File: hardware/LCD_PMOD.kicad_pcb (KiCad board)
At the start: 2 copper layers, 185 x 95 mm, 34 parts, among them IC1 TPS61169DCKR, IC2 TPD4E001DRLR, IC3 AR1021-I/SS, J1 20-pin power socket, J2 Conn_02x14_Odd_Even, J3 28-pin module socket, J4 691327310016, J5 691327310016, U1 ADS8556IPM, U2 OPA2211AIDDA, U3 DS90CF364AMTD, U4 DS90CF363AMTD

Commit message: Assigning footprints
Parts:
- removed J2: Conn_02x14_Odd_Even, Connector_PinHeader_2.54mm:PinHeader_2x14_P2.54mm_Horizontal
- added C10: 100n, Capacitor_SMD:C_0603_1608Metric, F.Cu at (110.5, 106.9)
- added C11: 100n, Capacitor_SMD:C_0603_1608Metric, F.Cu at (104.6, 107.7)
- added C12: 100n, Capacitor_SMD:C_0603_1608Metric, F.Cu at (116.8, 107.2)
- added C13: 100n, Capacitor_SMD:C_0603_1608Metric, F.Cu at (108.2, 114.3)
- added C14: 100n, Capacitor_SMD:C_0603_1608Metric, F.Cu at (117.3, 114.8)
- added C15: 100n, Capacitor_SMD:C_0603_1608Metric, F.Cu at (121.9, 108.0)
- added C16: 100n, Capacitor_SMD:C_0603_1608Metric, F.Cu at (113.0, 110.7)
- added C17: 100n, Capacitor_SMD:C_0603_1608Metric, F.Cu at (221.2, 102.6)
- added C18: 100n, Capacitor_SMD:C_0603_1608Metric, F.Cu at (210.6, 115.1)
- added C19: 100n, Capacitor_SMD:C_0603_1608Metric, F.Cu at (202.2, 105.2)
- added C20: 100n, Capacitor_SMD:C_0603_1608Metric, F.Cu at (209.1, 103.8)
- added C21: 100n, Capacitor_SMD:C_0603_1608Metric, F.Cu at (193.3, 110.0)
- added C22: 100n, Capacitor_SMD:C_0603_1608Metric, F.Cu at (202.4, 110.0)
- added C23: 100n, Capacitor_SMD:C_0603_1608Metric, F.Cu at (210.6, 98.6)
- added C24: 100n, Capacitor_SMD:C_0603_1608Metric, F.Cu at (199.4, 115.6)
- added C25: 100n, Capacitor_SMD:C_0603_1608Metric, F.Cu at (221.2, 115.3)
- added C26: 100n, Capacitor_SMD:C_0603_1608Metric, F.Cu at (209.0, 109.2)
- added C27: 100n, Capacitor_SMD:C_0603_1608Metric, F.Cu at (218.9, 108.7)
- added C28: 100n, Capacitor_SMD:C_0603_1608Metric, F.Cu at (206.0, 96.8)
- added C29: 100n, Capacitor_SMD:C_0603_1608Metric, F.Cu at (215.6, 113.5)
- added C30: 100n, Capacitor_SMD:C_0603_1608Metric, F.Cu at (204.7, 115.3)
- added C31: 100n, Capacitor_SMD:C_0603_1608Metric, F.Cu at (200.9, 100.8)
- added C32: 100n, Capacitor_SMD:C_0603_1608Metric, F.Cu at (215.1, 101.3)
- added C33: 100n, Capacitor_SMD:C_0603_1608Metric, F.Cu at (153.8, 55.7)
- added C34: 100n, Capacitor_SMD:C_0603_1608Metric, F.Cu at (143.3, 55.8)
- added C35: 100n, Capacitor_SMD:C_0603_1608Metric, F.Cu at (150.4, 60.5)
- added C36: 100n, Capacitor_SMD:C_0603_1608Metric, F.Cu at (93.1, 107.4)
- added C37: 10uF, Capacitor_SMD:C_0603_1608Metric, F.Cu at (90.1, 114.4)
- added C38: 100n, Capacitor_SMD:C_0603_1608Metric, F.Cu at (85.3, 111.8)
- added C39: 100n, Capacitor_SMD:C_0603_1608Metric, F.Cu at (150.2, 55.7)
- added C40: 470n, Capacitor_SMD:C_0603_1608Metric, F.Cu at (147.4, 60.5)
- added C41: 100n, Capacitor_SMD:C_0603_1608Metric, F.Cu at (87.6, 107.7)
- added C42: 100n, Capacitor_SMD:C_0603_1608Metric, F.Cu at (147.1, 55.9)
- added C43: 100n, Capacitor_SMD:C_0603_1608Metric, F.Cu at (95.8, 110.5)
- added C44: 1uF, Capacitor_SMD:C_0603_1608Metric, F.Cu at (144.4, 60.5)
- added C45: 10uF, Capacitor_SMD:C_0603_1608Metric, F.Cu at (98.8, 106.9)
- added C46: 100n, Capacitor_SMD:C_0603_1608Metric, F.Cu at (153.4, 60.5)
- added C47: 100n, Capacitor_SMD:C_0603_1608Metric, F.Cu at (93.1, 114.4)
- added C48: 10uF, Capacitor_SMD:C_0603_1608Metric, F.Cu at (100.6, 111.8)
- added C49: 10uF, Capacitor_SMD:C_0603_1608Metric, F.Cu at (104.9, 111.3)
- added C50: 10uF, Capacitor_SMD:C_0603_1608Metric, F.Cu at (96.1, 114.4)
- added C51: 10uF, Capacitor_SMD:C_0603_1608Metric, F.Cu at (103.6, 76.2)
- added C52: 100n, Capacitor_SMD:C_0603_1608Metric, F.Cu at (90.8, 80.1)
- added C53: 1u, Capacitor_SMD:C_0603_1608Metric, F.Cu at (89.9, 76.2)
- added C54: 22u, Capacitor_SMD:C_0603_1608Metric, F.Cu at (94.2, 78.2)
- added C55: 47u, Capacitor_SMD:C_0603_1608Metric, F.Cu at (97.7, 74.6)
- added C56: 47u, Capacitor_SMD:C_0603_1608Metric, F.Cu at (104.4, 71.9)
- added C57: 10n, Capacitor_SMD:C_0603_1608Metric, F.Cu at (94.5, 71.9)
- added C58: 10n, Capacitor_SMD:C_0603_1608Metric, F.Cu at (101.3, 83.3)
- added C59: 47u, Capacitor_SMD:C_0603_1608Metric, F.Cu at (99.8, 78.5)
- added C60: NI, Capacitor_SMD:C_0603_1608Metric, F.Cu at (287.3, 99.6)
- added C61: NI, Capacitor_SMD:C_0603_1608Metric, F.Cu at (249.0, 92.0)
- added C62: 370pF, Capacitor_SMD:C_0603_1608Metric, F.Cu at (265.7, 98.6)
- added C63: 470p, Capacitor_SMD:C_0603_1608Metric, F.Cu at (258.1, 84.3)
- added C64: 470p, Capacitor_SMD:C_0603_1608Metric, F.Cu at (268.0, 82.8)
- added C65: 1n, Capacitor_SMD:C_0603_1608Metric, F.Cu at (295.7, 99.3)
- added C66: 1n, Capacitor_SMD:C_0603_1608Metric, F.Cu at (261.4, 91.4)
- added C67: 270pF, Capacitor_SMD:C_0603_1608Metric, F.Cu at (249.4, 85.3)
- added C68: 270pF, Capacitor_SMD:C_0603_1608Metric, F.Cu at (274.6, 100.1)
- added C69: 270pF, Capacitor_SMD:C_0603_1608Metric, F.Cu at (278.6, 89.9)
- added C70: 270pF, Capacitor_SMD:C_0603_1608Metric, F.Cu at (270.7, 120.1)
- added C71: 22nF, Capacitor_SMD:C_0603_1608Metric, F.Cu at (248.8, 133.9)
- added C72: 22nF, Capacitor_SMD:C_0603_1608Metric, F.Cu at (253.0, 89.2)
- added C73: 100n, Capacitor_SMD:C_0603_1608Metric, F.Cu at (138.7, 115.4)
- added C9: 100n, Capacitor_SMD:C_0603_1608Metric, F.Cu at (122.2, 112.8)
- added IC4: TPD4E001-DRL, Package_TO_SOT_SMD:SOT-23-6, F.Cu at (87.8, 87.8)
- added IC5: TPD4E001-DRL, Package_TO_SOT_SMD:SOT-23-6, F.Cu at (94.1, 87.7)
- added IC6: M24C32-WMN6P, OPA2211:SOIC127P600X170-9N, F.Cu at (131.1, 111.9)
- added J6: Conn_02x10_Odd_Even, Connector_PinHeader_2.54mm:PinHeader_2x10_P2.54mm_Horizontal, F.Cu at (174.6, 123.2)
- added J7: JMP_A0, Connector_PinHeader_2.54mm:PinHeader_1x03_P2.54mm_Vertical, F.Cu at (107.5, 53.5)
- added J8: TBA1E, Connector_PinHeader_2.54mm:PinHeader_1x06_P2.54mm_Vertical, F.Cu at (175.1, 53.0)
- added R10: 1R, Resistor_SMD:R_0805_2012Metric, F.Cu at (85.6, 78.4)
- added R11: 10R, Resistor_SMD:R_0805_2012Metric, F.Cu at (97.3, 83.6)
- added R12: 100R, Resistor_SMD:R_0805_2012Metric, F.Cu at (90.9, 71.9)
- added R13: 49R9, Resistor_SMD:R_0805_2012Metric, F.Cu at (86.4, 73.7)
- added R14: R0, Resistor_SMD:R_0805_2012Metric, F.Cu at (194.3, 78.9)
- added R15: R0, Resistor_SMD:R_0805_2012Metric, F.Cu at (206.8, 68.8)
- added R16: R0, Resistor_SMD:R_0805_2012Metric, F.Cu at (207.5, 72.9)
- added R17: R0, Resistor_SMD:R_0805_2012Metric, F.Cu at (194.8, 73.7)
- added R18: R0, Resistor_SMD:R_0805_2012Metric, F.Cu at (199.6, 69.3)
- added R19: R0, Resistor_SMD:R_0805_2012Metric, F.Cu at (209.8, 77.7)
- added R20: R0, Resistor_SMD:R_0805_2012Metric, F.Cu at (201.9, 73.7)
- added R21: R0, Resistor_SMD:R_0805_2012Metric, F.Cu at (213.6, 74.2)
- added R22: R0, Resistor_SMD:R_0805_2012Metric, F.Cu at (194.3, 69.6)
- added R23: R0, Resistor_SMD:R_0805_2012Metric, F.Cu at (213.4, 68.8)
- added R24: 49R9, Resistor_SMD:R_0805_2012Metric, F.Cu at (258.3, 125.2)
- added R25: NI, Resistor_SMD:R_0805_2012Metric, F.Cu at (248.2, 128.7)
- added R26: 49R9, Resistor_SMD:R_0805_2012Metric, F.Cu at (264.1, 129.5)
- added R27: 49R9, Resistor_SMD:R_0805_2012Metric, F.Cu at (274.1, 81.8)
- added R28: 1K2, Resistor_SMD:R_0805_2012Metric, F.Cu at (237.1, 141.5)
- added R29: 1K2, Resistor_SMD:R_0805_2012Metric, F.Cu at (245.5, 148.8)
- added R30: 1K2, Resistor_SMD:R_0805_2012Metric, F.Cu at (283.7, 80.8)
- added R31: 1K2, Resistor_SMD:R_0805_2012Metric, F.Cu at (247.9, 79.2)
- added R32: 1K, Resistor_SMD:R_0805_2012Metric, F.Cu at (278.1, 124.0)
- added R33: 300R, Resistor_SMD:R_0805_2012Metric, F.Cu at (294.9, 91.2)
- added R34: 300R, Resistor_SMD:R_0805_2012Metric, F.Cu at (234.7, 148.1)
- added R35: 1K, Resistor_SMD:R_0805_2012Metric, F.Cu at (244.9, 84.8)
- added R36: 300R, Resistor_SMD:R_0805_2012Metric, F.Cu at (245.0, 143.2)
- added R37: 300R, Resistor_SMD:R_0805_2012Metric, F.Cu at (275.8, 129.3)
- added R38: 1K2, Resistor_SMD:R_0805_2012Metric, F.Cu at (252.4, 143.8)
- added R39: 1K2, Resistor_SMD:R_0805_2012Metric, F.Cu at (258.6, 79.2)
- added R40: 1K2, Resistor_SMD:R_0805_2012Metric, F.Cu at (257.0, 149.4)
- added R41: 1K2, Resistor_SMD:R_0805_2012Metric, F.Cu at (288.1, 88.1)
- added R42: 5R, Resistor_SMD:R_0805_2012Metric, F.Cu at (262.1, 84.8)
- added R43: 5R, Resistor_SMD:R_0805_2012Metric, F.Cu at (267.9, 89.2)
- added R44: 5R, Resistor_SMD:R_0805_2012Metric, F.Cu at (267.1, 93.0)
- added R45: 5R, Resistor_SMD:R_0805_2012Metric, F.Cu at (253.0, 80.8)
- added R46: 10R, Resistor_SMD:R_0805_2012Metric, F.Cu at (250.2, 148.8)
- added R47: 10R, Resistor_SMD:R_0805_2012Metric, F.Cu at (243.1, 90.2)
- added R48: 10R, Resistor_SMD:R_0805_2012Metric, F.Cu at (261.1, 119.1)
- added R49: 10R, Resistor_SMD:R_0805_2012Metric, F.Cu at (292.9, 83.3)
- added R50: 10K, Capacitor_SMD:C_0805_2012Metric, F.Cu at (142.2, 110.5)
- added R51: 10K, Capacitor_SMD:C_0805_2012Metric, F.Cu at (149.0, 110.5)
- added R52: 10K, Capacitor_SMD:C_0805_2012Metric, F.Cu at (145.6, 110.5)
- added R6: 100, Resistor_SMD:R_0805_2012Metric, F.Cu at (195.6, 100.6)
- added R7: 100, Resistor_SMD:R_0805_2012Metric, F.Cu at (195.6, 105.4)
- added R8: 100, Resistor_SMD:R_0805_2012Metric, F.Cu at (214.4, 107.7)
- added R9: 100, Resistor_SMD:R_0805_2012Metric, F.Cu at (197.9, 109.2)
- added U5: OPA2211AIDDA, OPA2211:SOIC127P600X170-9N, F.Cu at (159.8, 76.2)
- added U6: THS4032ID, EEZ DIB MCU r1B1:SOIC127P600X173-8N, F.Cu at (88.4, 63.8)
- added U7: THS4551IDGKT, Package_SO:VSSOP-8_3.0x3.0mm_P0.65mm, F.Cu at (95.4, 55.0)
- added U8: THS4551IDGKT, Package_SO:VSSOP-8_3.0x3.0mm_P0.65mm, F.Cu at (109.3, 61.4)
- C1: footprint EEZ DIB MCU r1B1:C1206 -> Capacitor_SMD:C_1206_3216Metric
- C2, C7: footprint EEZ DIB MCU r1B1:C0603 -> Capacitor_SMD:C_0603_1608Metric
- C3, C4, C5, C6, C8: footprint EEZ DIB MCU r1B1:C0805 -> Capacitor_SMD:C_0805_2012Metric
- TOUCH1: value HSMY-C170 -> LED; footprint EEZ DIB MCU r1B1:LED_0805 -> LED_SMD:LED_0603_1608Metric
- U2: value OPA2211AIDDA -> REF5025AD; footprint OPA2211:SOIC127P600X170-9N -> Package_SO:SOIC-8_3.9x4.9mm_P1.27mm
- moved R1 50.9 mm to (144.3, 85.8)
- moved C7 49.6 mm to (136.4, 97.9)
- moved C1 49.6 mm to (153.7, 91.3)
- moved C6 49.6 mm to (145.1, 90.8)
- moved IC1 49.6 mm to (158.5, 96.4)
- moved IC2 49.6 mm to (155.0, 99.2)
- moved R2 49.6 mm to (148.1, 98.2)
- moved R3 49.6 mm to (139.5, 90.8)
- moved R4 49.6 mm to (148.1, 90.7)
- moved R5 49.6 mm to (136.4, 90.8)
- moved TOUCH1 49.6 mm to (142.8, 98.2)
- moved C2 49.6 mm to (139.2, 98.0)
- moved C3 49.6 mm to (150.7, 90.8)
- moved C4 49.6 mm to (142.3, 90.8)
- moved C5 49.6 mm to (150.7, 98.2)
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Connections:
- C1 pad 1: +5V -> 5V
- C1 pad 2: GND -> A1_IN
- C2 pad 1: GND -> A1_IN
- C2 pad 2: +3V3 -> 3V3
- C3 pad 1: /LCD/VLED+ -> VLED+
- C3 pad 2: GND -> A1_IN
- C4 pad 2: GND -> A1_IN
- C5 pad 1: +3V3 -> 3V3
- C5 pad 2: GND -> A1_IN
- C6 pad 2: GND -> A1_IN
- C7 pad 1: GND -> A1_IN
- C7 pad 2: +3V3 -> 3V3
- C8 pad 1: GND -> A1_IN
- C8 pad 2: +3V3 -> 3V3
- D1 pad C: /LCD/VLED+ -> VLED+
- IC1 pad 2: GND -> A1_IN
- IC1 pad 3: /LCD/VLED- -> VLED-
- IC1 pad 4: (no net) -> 8N
- IC2 pad 3: GND -> A1_IN
- IC2 pad 6: +3V3 -> 3V3
- IC3 pad 1: +3V3 -> 3V3
- IC3 pad 11: (no net) -> 7P
- IC3 pad 13: (no net) -> 7N
- IC3 pad 14: GND -> A1_IN
- IC3 pad 17: GND -> A1_IN
- IC3 pad 2: GND -> A1_IN
- IC3 pad 20: GND -> A1_IN
- IC3 pad 3: GND -> A1_IN
- IC3 pad 4: GND -> A1_IN
- IC3 pad 7: GND -> A1_IN
- IC3 pad 9: (no net) -> 8P
- J3 pad 10: (no net) -> 0N
- J3 pad 11: (no net) -> 0P
- J3 pad 12: GND -> A1_IN
- J3 pad 13: (no net) -> 1N
- J3 pad 14: (no net) -> 2N
- J3 pad 15: GND -> A1_IN
- J3 pad 16: (no net) -> 1P
- J3 pad 17: (no net) -> A2
- J3 pad 18: (no net) -> A0
- J3 pad 19: GND -> A1_IN
- J3 pad 2: +3V3 -> (no net)
- J3 pad 20: (no net) -> A1
- J3 pad 23: +5V -> 5V
- J3 pad 24: +5V -> 5V
- J3 pad 26: GND -> A1_IN
- J3 pad 3: (no net) -> 13N
- J3 pad 6: (no net) -> SSCL
- J3 pad 7: (no net) -> SSDA
- J3 pad 8: GND -> A1_IN
- J3 pad 9: (no net) -> 2P
- J4 pad 1: (no net) -> A0_IN
- J4 pad 10: (no net) -> B1_IN
- J4 pad 11: (no net) -> C1_IN
- J4 pad 2: (no net) -> B0_IN
- J4 pad 3: (no net) -> C0_IN
- J4 pad 9: (no net) -> A1_IN
- JP1 pad NC: (no net) -> 13N
- JP1 pad NO: GND -> A1_IN
- L1 pad 1: +5V -> 5V
- LCD_IN1 pad 1: (no net) -> VLED-
- LCD_IN1 pad 13: GND -> A1_IN
- LCD_IN1 pad 14: GND -> A1_IN
- LCD_IN1 pad 2: (no net) -> VLED+
- LCD_IN1 pad 21: GND -> A1_IN
- LCD_IN1 pad 22: GND -> A1_IN
- LCD_IN1 pad 29: GND -> A1_IN
- LCD_IN1 pad 3: GND -> A1_IN
- LCD_IN1 pad 5: GND -> A1_IN
- LCD_IN1 pad 6: GND -> A1_IN
- LCD_OUT1 pad 1: /LCD/VLED- -> VLED-
- LCD_OUT1 pad 13: GND -> A1_IN
- LCD_OUT1 pad 14: GND -> A1_IN
- LCD_OUT1 pad 2: /LCD/VLED+ -> VLED+
- LCD_OUT1 pad 21: GND -> A1_IN
- LCD_OUT1 pad 22: GND -> A1_IN
- LCD_OUT1 pad 29: GND -> A1_IN
- LCD_OUT1 pad 3: GND -> A1_IN
- LCD_OUT1 pad 4: +3V3 -> 3V3
- LCD_OUT1 pad 5: GND -> A1_IN
- LCD_OUT1 pad 6: GND -> A1_IN
- R1 pad 1: +5V -> 5V
- R2 pad 1: /LCD/VLED- -> VLED-
- R2 pad 2: GND -> A1_IN
- R3 pad 2: +3V3 -> 3V3
- U1 pad 1: (no net) -> 18N
- U1 pad 10: (no net) -> 22P
- U1 pad 11: (no net) -> 22N
- U1 pad 12: (no net) -> 23P
- U1 pad 13: (no net) -> 23N
- U1 pad 14: (no net) -> 24P
- U1 pad 15: (no net) -> 24N
- U1 pad 16: (no net) -> 25P
- U1 pad 17: (no net) -> 25N
- U1 pad 19: (no net) -> 26N
- U1 pad 2: (no net) -> 19P
- U1 pad 20: (no net) -> 26P
- U1 pad 21: (no net) -> 27P
- U1 pad 22: (no net) -> 27P
- U1 pad 23: (no net) -> 27P
- U1 pad 24: (no net) -> 5V
- U1 pad 25: (no net) -> A1_IN
- U1 pad 26: (no net) -> 5V
- U1 pad 27: (no net) -> ADC_RANGE
- U1 pad 28: (no net) -> 27N
- U1 pad 29: (no net) -> ADC_WORD
- U1 pad 3: (no net) -> 19N
- U1 pad 30: (no net) -> HVSS
- U1 pad 31: (no net) -> HVDD
- U1 pad 32: (no net) -> A1_IN
- U1 pad 33: (no net) -> ADC_A0
- U1 pad 34: (no net) -> 5V
- U1 pad 35: (no net) -> 5V
- U1 pad 37: (no net) -> A1_IN
- U1 pad 38: (no net) -> A1_IN
- U1 pad 39: (no net) -> ADC_B0
- U1 pad 4: (no net) -> 20P
- U1 pad 40: (no net) -> 5V
- U1 pad 41: (no net) -> 5V
- U1 pad 42: (no net) -> ADC_B1
- U1 pad 43: (no net) -> A1_IN
- U1 pad 44: (no net) -> A1_IN
- U1 pad 45: (no net) -> ADC_C0
- U1 pad 46: (no net) -> 5V
- U1 pad 47: (no net) -> 5V
- U1 pad 48: (no net) -> ADC_C1
- U1 pad 49: (no net) -> A1_IN
- U1 pad 5: (no net) -> 20N
- U1 pad 50: (no net) -> 5V
- U1 pad 51: (no net) -> ADC_REF
- U1 pad 52: (no net) -> A1_IN
- U1 pad 53: (no net) -> A1_IN
- U1 pad 54: (no net) -> Net-(C49-Pad2)
- U1 pad 55: (no net) -> A1_IN
- U1 pad 56: (no net) -> Net-(C48-Pad2)
- U1 pad 57: (no net) -> A1_IN
- U1 pad 58: (no net) -> Net-(C50-Pad2)
- U1 pad 59: (no net) -> A1_IN
- U1 pad 6: (no net) -> 21P
- U1 pad 60: (no net) -> 5V
- U1 pad 61: (no net) -> ADC_PAR
- U1 pad 62: (no net) -> ADC_HW_SW
- U1 pad 63: (no net) -> ADC_REF_EN_WR
- U1 pad 64: (no net) -> 18P
- U1 pad 7: (no net) -> 21N
- U1 pad 9: (no net) -> 3V3
- U2 pad 2: (no net) -> 5V
- U2 pad 4: (no net) -> A1_IN
- U2 pad 5: (no net) -> Net-(C53-Pad1)
- U2 pad 6: (no net) -> Net-(R10-Pad1)
- U3 pad 10: (no net) -> 4N
- U3 pad 11: (no net) -> 4P
- U3 pad 12: (no net) -> 3V3
- U3 pad 13: (no net) -> A1_IN
- U3 pad 14: (no net) -> 5N
- U3 pad 15: (no net) -> 5P
- U3 pad 16: (no net) -> 6N
- U3 pad 17: (no net) -> 6P
- U3 pad 18: (no net) -> A1_IN
- U3 pad 19: (no net) -> A1_IN
- U3 pad 20: (no net) -> 3V3
- U3 pad 21: (no net) -> A1_IN
- U3 pad 22: (no net) -> 13N
- U3 pad 25: (no net) -> A1_IN
- U3 pad 28: (no net) -> 3V3
- U3 pad 3: (no net) -> A1_IN
- U3 pad 32: (no net) -> A1_IN
- U3 pad 36: (no net) -> 3V3
- U3 pad 38: (no net) -> A1_IN
- U3 pad 42: (no net) -> 3V3
- U3 pad 44: (no net) -> A1_IN
- U3 pad 48: (no net) -> 3V3
- U3 pad 7: (no net) -> A1_IN
- U3 pad 8: (no net) -> 3N
- U3 pad 9: (no net) -> 3P
- U4 pad 11: GND -> A1_IN
- U4 pad 17: GND -> A1_IN
- U4 pad 24: GND -> A1_IN
- U4 pad 28: GND -> A1_IN
- U4 pad 30: GND -> A1_IN
- U4 pad 31: GND -> A1_IN
- U4 pad 32: 12P -> Net-(C28-Pad2)
- U4 pad 33: 12N -> Net-(C32-Pad2)
- U4 pad 34: (no net) -> Net-(C27-Pad2)
- U4 pad 35: (no net) -> Net-(C31-Pad2)
- U4 pad 36: GND -> A1_IN
- U4 pad 38: 10P -> Net-(C26-Pad2)
- U4 pad 39: 10N -> Net-(C30-Pad2)
- U4 pad 40: 9P -> Net-(C25-Pad2)
- U4 pad 41: 9N -> Net-(C29-Pad2)
- U4 pad 42: GND -> A1_IN
- U4 pad 46: GND -> A1_IN
- U4 pad 5: GND -> A1_IN
- ULX3S_L1 pad 10: (no net) -> 2P
- ULX3S_L1 pad 11: (no net) -> 3N
- ULX3S_L1 pad 12: (no net) -> 3P
- ULX3S_L1 pad 13: (no net) -> 4N
- ULX3S_L1 pad 14: (no net) -> 4P
- ULX3S_L1 pad 15: (no net) -> 5N
- ULX3S_L1 pad 16: (no net) -> 5P
- ULX3S_L1 pad 17: (no net) -> 6N
- ULX3S_L1 pad 18: (no net) -> 6P
- ULX3S_L1 pad 21: GND -> A1_IN
- ULX3S_L1 pad 22: GND -> A1_IN
- ULX3S_L1 pad 23: (no net) -> 7N
- ULX3S_L1 pad 24: (no net) -> 7P
- ULX3S_L1 pad 25: (no net) -> 8N
- ULX3S_L1 pad 26: (no net) -> 8P
- ULX3S_L1 pad 3: GND -> A1_IN
- ULX3S_L1 pad 31: (no net) -> 11N
- ULX3S_L1 pad 32: (no net) -> 11P
- ULX3S_L1 pad 35: (no net) -> 13N
- ULX3S_L1 pad 37: GND -> A1_IN
- ULX3S_L1 pad 38: GND -> A1_IN
- ULX3S_L1 pad 4: GND -> A1_IN
- ULX3S_L1 pad 5: (no net) -> 0N
- ULX3S_L1 pad 6: (no net) -> 0P
- ULX3S_L1 pad 7: (no net) -> 1N
- ULX3S_L1 pad 8: (no net) -> 1P
- ULX3S_L1 pad 9: (no net) -> 2N
- ULX3S_R1 pad 10: (no net) -> 25N
- ULX3S_R1 pad 11: (no net) -> 24P
- ULX3S_R1 pad 12: (no net) -> 24N
- ULX3S_R1 pad 13: (no net) -> 23P
- ULX3S_R1 pad 14: (no net) -> 23N
- ULX3S_R1 pad 15: (no net) -> 22P
- ULX3S_R1 pad 16: (no net) -> 22N
- ULX3S_R1 pad 17: (no net) -> 21P
- ULX3S_R1 pad 18: (no net) -> 21N
- ULX3S_R1 pad 19: GND -> A1_IN
- ULX3S_R1 pad 20: GND -> A1_IN
- ULX3S_R1 pad 23: (no net) -> 20P
- ULX3S_R1 pad 24: (no net) -> 20N
- ULX3S_R1 pad 25: (no net) -> 19P
- ULX3S_R1 pad 26: (no net) -> 19N
- ULX3S_R1 pad 27: (no net) -> 18P
- ULX3S_R1 pad 28: (no net) -> 18N
- ULX3S_R1 pad 3: GND -> A1_IN
- ULX3S_R1 pad 37: GND -> A1_IN
- ULX3S_R1 pad 38: GND -> A1_IN
- ULX3S_R1 pad 4: GND -> A1_IN
- ULX3S_R1 pad 5: (no net) -> 27P
- ULX3S_R1 pad 6: (no net) -> 27N
- ULX3S_R1 pad 7: (no net) -> 26P
- ULX3S_R1 pad 8: (no net) -> 26N
- ULX3S_R1 pad 9: (no net) -> 25P
- ZD1 pad A: /LCD/VLED- -> VLED-
- ZD1 pad C: /LCD/VLED+ -> VLED+
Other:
- board size 185 x 95 mm -> 175.1 x 95 mm

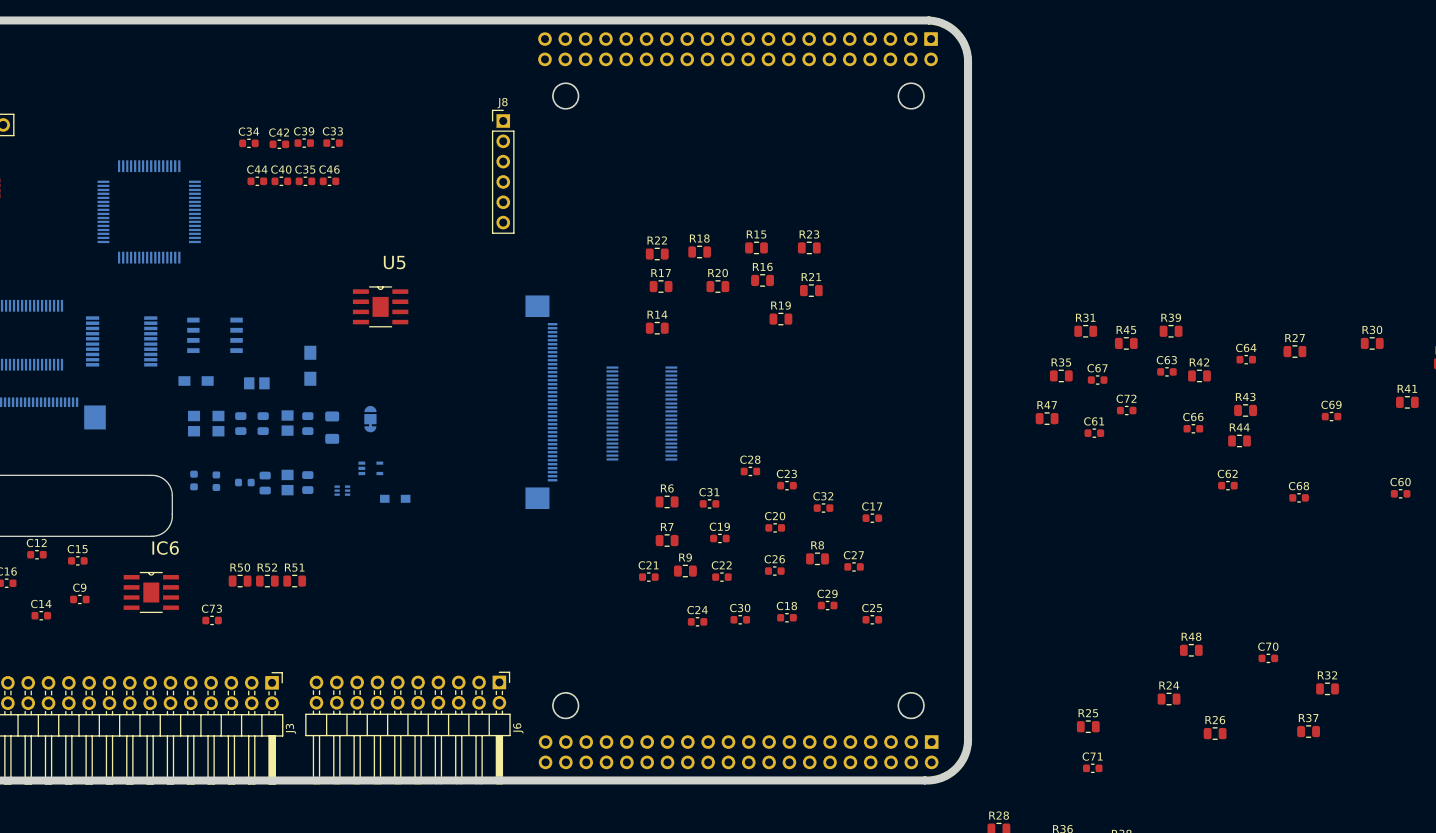
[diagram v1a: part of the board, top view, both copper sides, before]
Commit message: Adding chip power down fix - removing ADS8556 chip
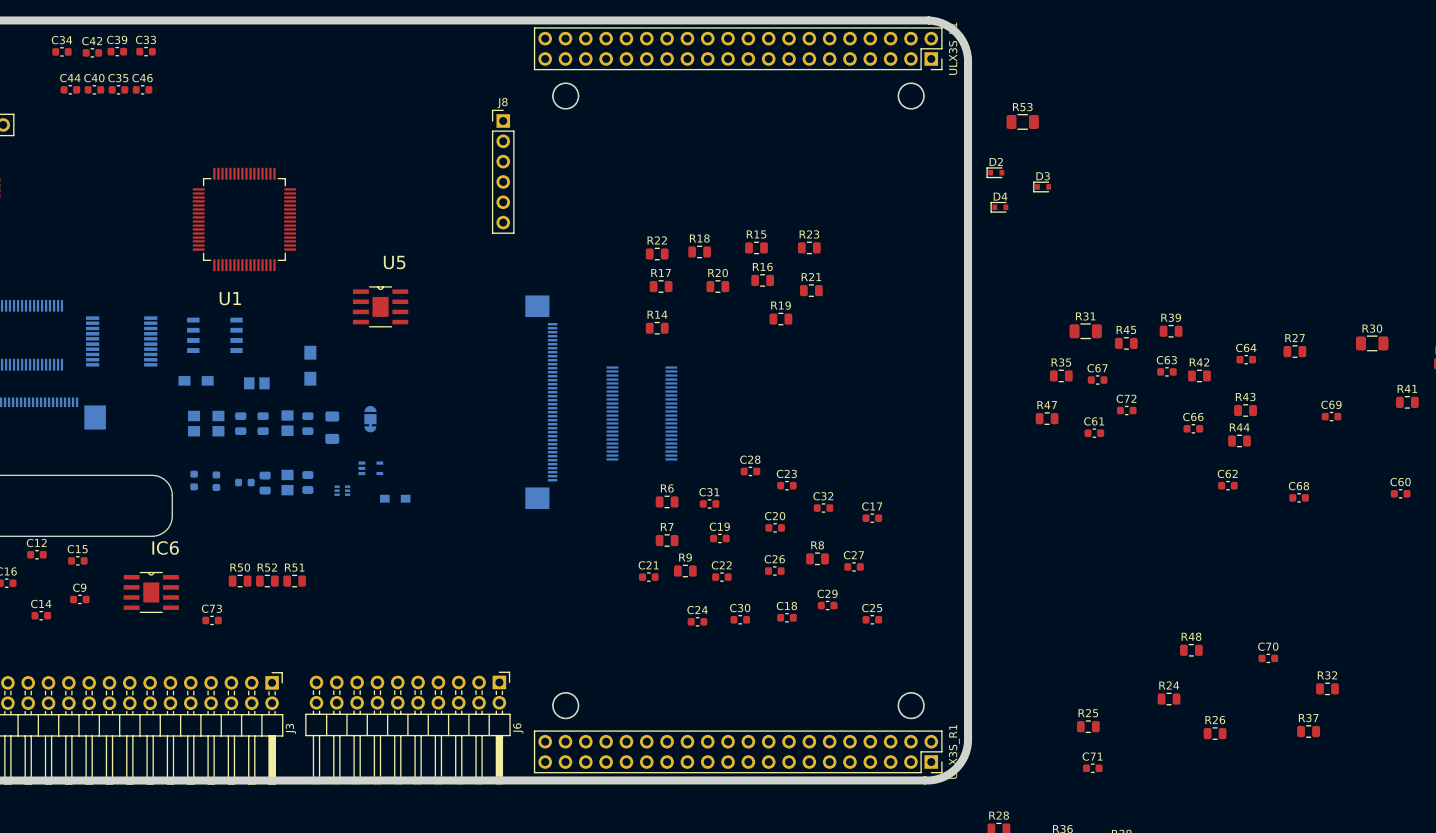
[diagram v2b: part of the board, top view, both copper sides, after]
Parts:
- added D2: D_TVS, Diode_SMD:D_SOD-523, F.Cu at (236.7, 59.4)
- added D3: D_TVS, Diode_SMD:D_SOD-523, F.Cu at (242.6, 61.2)
- added D4: D_TVS, Diode_SMD:D_SOD-523, F.Cu at (237.2, 63.8)
- added R53: 1K, Resistor_SMD:R_1206_3216Metric, F.Cu at (240.0, 53.1)
- R30, R31: footprint Resistor_SMD:R_0805_2012Metric -> Resistor_SMD:R_1206_3216Metric
- U1, ULX3S_L1, ULX3S_R1: moved to F.Cu
- moved ULX3S_R1 90.4 mm to (228.6, 133.1), turned to 270 degrees
- moved ULX3S_L1 85.4 mm to (228.6, 45.2), turned to 270 degrees
- moved C34 26.0 mm to (119.9, 44.3)
- moved C40 26.0 mm to (124.0, 49.1)
- moved C42 26.0 mm to (123.7, 44.5)
- moved C33 26.0 mm to (130.5, 44.3)
- moved C35 26.0 mm to (127.0, 49.1)
- moved C39 26.0 mm to (126.9, 44.3)
- moved C46 26.0 mm to (130.0, 49.1)
- moved C44 26.0 mm to (121.0, 49.1)
- moved U1 11.9 mm to (142.7, 65.3), turned to 180 degrees
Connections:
- J7 pad 2: A0_IN -> Net-(D2-Pad1)
- R24 pad 2: A0_IN -> Net-(D2-Pad1)

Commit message: Adding last known changes to shematics
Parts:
- LCD_OUT1, U3: moved to F.Cu
- U1: moved to B.Cu
- moved U3 49.2 mm to (158.7, 58.7), turned to 180 degrees
- moved LCD_OUT1 15.8 mm to (111.6, 74.2), turned to 0 degrees
- moved IC3 15.2 mm to (123.2, 95.1)
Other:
- board size 175.1 x 95 mm -> 215.1 x 95 mm

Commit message: Routing board
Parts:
- removed C15, C16, C41, C42, C43, C46, C47, C52, C73: 100n, Capacitor_SMD:C_0603_1608Metric
- removed C40: 470n, Capacitor_SMD:C_0603_1608Metric
- removed C44: 1uF, Capacitor_SMD:C_0603_1608Metric
- removed C45, C48, C49, C50: 10uF, Capacitor_SMD:C_0603_1608Metric
- removed C53: 1u, Capacitor_SMD:C_0603_1608Metric
- removed C56, C59: 47u, Capacitor_SMD:C_0603_1608Metric
- removed C57, C58: 10n, Capacitor_SMD:C_0603_1608Metric
- removed IC5: TPD4E001-DRL, Package_TO_SOT_SMD:SOT-23-6
- removed IC6: M24C32-WMN6P, OPA2211:SOIC127P600X170-9N
- removed U5: OPA2211AIDDA, OPA2211:SOIC127P600X170-9N
- added D5: D_TVS, Diode_SMD:D_SOD-523, F.Cu at (92.2, 89.2)
- added D6: D_TVS, Diode_SMD:D_SOD-523, B.Cu at (90.6, 82.7)
- added D7: D_TVS, Diode_SMD:D_SOD-523, B.Cu at (90.6, 74.1)
- added H1: L_H, MountingHole:MountingHole_3.5mm_Pad_Via, F.Cu at (173.2, 55.6)
- added H2: L_H, MountingHole:MountingHole_3.5mm_Pad_Via, F.Cu at (173.2, 114.3)
- added H3: L_H, MountingHole:MountingHole_3.5mm_Pad_Via, F.Cu at (87.9, 55.6)
- added H4: L_H, MountingHole:MountingHole_3.5mm_Pad_Via, F.Cu at (87.9, 114.6)
- added J10: OS0, Connector_PinHeader_2.00mm:PinHeader_1x03_P2.00mm_Vertical, F.Cu at (152.3, 43.8)
- added J11: OS1, Connector_PinHeader_2.00mm:PinHeader_1x03_P2.00mm_Vertical, F.Cu at (155.4, 43.8)
- added J12: OS2, Connector_PinHeader_2.00mm:PinHeader_1x03_P2.00mm_Vertical, F.Cu at (158.4, 43.8)
- added J13: PAR, Connector_PinHeader_2.00mm:PinHeader_1x03_P2.00mm_Vertical, F.Cu at (161.5, 43.8)
- added J14: RANGE, Connector_PinHeader_2.00mm:PinHeader_1x03_P2.00mm_Vertical, F.Cu at (164.5, 43.8)
- added J15: REF, Connector_PinHeader_2.00mm:PinHeader_1x03_P2.00mm_Vertical, F.Cu at (167.6, 43.8)
- added J16: TBA1E, TBA1E:TBA1E, F.Cu at (128.5, 44.7)
- added J17: FTDI, Connector_PinHeader_2.54mm:PinHeader_2x03_P2.54mm_Vertical, F.Cu at (159.5, 108.0)
- added J2: VS_SCL, Connector_PinHeader_2.00mm:PinHeader_1x03_P2.00mm_Vertical, F.Cu at (171.6, 43.9)
- added J9: DIB_V2, Connector_PinHeader_2.54mm:PinHeader_2x10_P2.54mm_Horizontal, F.Cu at (175.0, 123.0)
- added R54: 1K, Resistor_SMD:R_1206_3216Metric, F.Cu at (95.5, 89.2)
- C10, C11, C12, C13, C14, C25, C34, C35, C39, C63, C64, C65, C66, C67, C68, C69, C70, C71, C72, C9, D3, D4, R30, R31, R32, R35, R38, R39, R40, R41, R42, R43, R44, R45, R46, R47, R48, R49, R6, R7, R8, R9, U7, U8: moved to B.Cu
- C2, C7, C8, IC2, IC3, JP1, TOUCH1, U2: moved to F.Cu
- C26, C28, C29: value 100n -> 10uF; footprint Capacitor_SMD:C_0603_1608Metric -> Capacitor_SMD:C_0805_2012Metric
- C27: value 100n -> 1u/X7R-grade; footprint Capacitor_SMD:C_0603_1608Metric -> Capacitor_SMD:C_0805_2012Metric
- C31: value 100n -> CP; footprint Capacitor_SMD:C_0603_1608Metric -> Capacitor_SMD:C_0805_2012Metric
- C36: value 100n -> CP; footprint Capacitor_SMD:C_0603_1608Metric -> Capacitor_Tantalum_SMD:CP_EIA-3528-21_Kemet-B
- C37: value 10uF -> 1nF
- C51: value 10uF -> 1uF
- C54: value 22u -> 10u
- C55: value 47u -> 10u
- IC4: value TPD4E001-DRL -> M24C32-WMN6P; footprint Package_TO_SOT_SMD:SOT-23-6 -> OPA2211:SOIC127P600X170-9N; moved to B.Cu
- J6: value Conn_02x10_Odd_Even -> HS_SDA; footprint Connector_PinHeader_2.54mm:PinHeader_2x10_P2.54mm_Horizontal -> Connector_PinHeader_2.00mm:PinHeader_1x03_P2.00mm_Vertical
- J7: footprint Connector_PinHeader_2.54mm:PinHeader_1x03_P2.54mm_Vertical -> Connector_PinHeader_2.00mm:PinHeader_1x03_P2.00mm_Vertical
- J8: value TBA1E -> DE_IRQ; footprint Connector_PinHeader_2.54mm:PinHeader_1x06_P2.54mm_Vertical -> Connector_PinHeader_2.00mm:PinHeader_1x03_P2.00mm_Vertical
- R1, R2, R3, R4: footprint EEZ DIB MCU r1B1:R0805 -> Resistor_SMD:R_0805_2012Metric
- R10: value 1R -> 0,22R
- R11: value 10R -> 100R
- R12: value 100R -> 10K; moved to B.Cu
- R13: value 49R9 -> 10K; footprint Resistor_SMD:R_0805_2012Metric -> Capacitor_SMD:C_0805_2012Metric; moved to B.Cu
- R14, R15: value R0 -> 10K; footprint Resistor_SMD:R_0805_2012Metric -> Capacitor_SMD:C_0805_2012Metric; moved to B.Cu
- R16: value R0 -> 10K; moved to B.Cu
- R17, R18, R19, R20, R21, R22: value R0 -> 1K
- R23: value R0 -> 1K; moved to B.Cu
- R24: footprint Resistor_SMD:R_0805_2012Metric -> Resistor_SMD:R_1206_3216Metric
- R28, R29, R33, R34, R36, R37: footprint Resistor_SMD:R_0805_2012Metric -> Resistor_SMD:R_1206_3216Metric; moved to B.Cu
- R5: footprint EEZ DIB MCU r1B1:R0805 -> Resistor_SMD:R_0805_2012Metric; moved to F.Cu
- R50: value 10K -> 49R9; footprint Capacitor_SMD:C_0805_2012Metric -> Resistor_SMD:R_0805_2012Metric
- R51, R52: value 10K -> 1K; footprint Capacitor_SMD:C_0805_2012Metric -> Resistor_SMD:R_1206_3216Metric
- U1: value ADS8556IPM -> ADS8586S; footprint ADS8556IPM:QFP50P1200X1200X160-64N -> Package_QFP:LQFP-64_10x10mm_P0.5mm; moved to F.Cu
- U4: value DS90CF363AMTD -> DS90CF36B
- moved R30 194.6 mm to (89.6, 67.0), turned to 180 degrees
- moved R33 192.2 mm to (103.1, 79.5), turned to 180 degrees
- moved C65 187.6 mm to (109.3, 78.2), turned to 270 degrees
- moved R41 187.4 mm to (102.6, 61.5), turned to 180 degrees
- moved C60 186.7 mm to (105.7, 56.1), turned to 270 degrees
- moved R37 184.5 mm to (103.0, 64.5), turned to 180 degrees
- moved R26 176.0 mm to (105.9, 52.3), turned to 180 degrees
- moved R40 173.6 mm to (102.6, 70.1), turned to 180 degrees
- moved R32 172.8 mm to (110.4, 82.4)
- moved R24 172.5 mm to (101.9, 52.6), turned to 180 degrees
- moved C64 172.0 mm to (96.8, 65.7), turned to 270 degrees
- moved R29 171.5 mm to (89.8, 77.1), turned to 180 degrees
- moved C69 166.9 mm to (114.2, 61.5)
- moved C70 164.3 mm to (114.2, 70.1)
- moved R49 164.0 mm to (129.7, 66.8), turned to 180 degrees
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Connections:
- net /Video_IN/VSYNC renamed STM32_VSYNC
- net C0_IN renamed A4_IN_P
- net C1_IN renamed A4_IN_N
- net Net-(C63-Pad1) renamed /ADC/ADC_buffer/A4N
- net Net-(C63-Pad2) renamed /ADC/ADC_buffer/A4P
- net Net-(C64-Pad1) renamed /ADC/ADC_buffer/A2N
- net Net-(C64-Pad2) renamed /ADC/ADC_buffer/A2P
- net Net-(C65-Pad1) renamed /ADC/ADC_buffer/U7N
- net Net-(C65-Pad2) renamed /ADC/ADC_buffer/U7P
- net Net-(C66-Pad1) renamed /ADC/ADC_buffer/U8N
- net Net-(C66-Pad2) renamed /ADC/ADC_buffer/U8P
- net Net-(C67-Pad2) renamed /ADC/ADC_buffer/A4_out+
- net Net-(C68-Pad2) renamed /ADC/ADC_buffer/A4_out-
- net Net-(C69-Pad2) renamed /ADC/ADC_buffer/A2_out+
- net Net-(C70-Pad2) renamed /ADC/ADC_buffer/A2_out-
- net Net-(R38-Pad1) renamed /ADC/ADC_buffer/A4_out2+
- net Net-(R39-Pad1) renamed /ADC/ADC_buffer/A4_out2-
- net Net-(R40-Pad1) renamed /ADC/ADC_buffer/A2_out2+
- net Net-(R41-Pad1) renamed /ADC/ADC_buffer/A2_out2-
- C1 pad 2: A1_IN -> ADC_REFGND
- C10 pad 2: A1_IN -> ADC_REFGND
- C11 pad 2: A1_IN -> ADC_REFGND
- C12 pad 2: A1_IN -> ADC_REFGND
- C13 pad 2: A1_IN -> ADC_REFGND
- C14 pad 2: A1_IN -> ADC_REFGND
- C17 pad 2: A1_IN -> ADC_REFGND
- C18 pad 2: A1_IN -> ADC_REFGND
- C19 pad 2: A1_IN -> ADC_REFGND
- C2 pad 1: A1_IN -> ADC_REFGND
- C20 pad 2: A1_IN -> ADC_REFGND
- C21 pad 2: A1_IN -> ADC_REFGND
- C22 pad 2: A1_IN -> ADC_REFGND
- C23 pad 2: A1_IN -> ADC_REFGND
- C24 pad 2: A1_IN -> ADC_REFGND
- C25 pad 1: 9P -> ADC_REFGND
- C25 pad 2: Net-(C25-Pad2) -> DIB_+3V3
- C26 pad 1: 10P -> Net-(C26-Pad1)
- C26 pad 2: Net-(C26-Pad2) -> ADC_REFGND
- C27 pad 1: 11P -> ADC_REFGND
- C28 pad 1: 12P -> ADC_REFGND
- C29 pad 1: 9N -> ADC_REF
- C29 pad 2: Net-(C29-Pad2) -> ADC_REFGND
- C3 pad 2: A1_IN -> ADC_REFGND
- C30 pad 1: 10N -> HVDD
- C30 pad 2: Net-(C30-Pad2) -> ADC_REFGND
- C31 pad 1: 11N -> HVDD
- C31 pad 2: Net-(C31-Pad2) -> ADC_REFGND
- C32 pad 1: 12N -> HVSS
- C32 pad 2: Net-(C32-Pad2) -> ADC_REFGND
- C33 pad 2: A1_IN -> ADC_REFGND
- C34 pad 2: A1_IN -> ADC_REFGND
- C35 pad 2: A1_IN -> ADC_REFGND
- C36 pad 1: HVDD -> HVSS
- C36 pad 2: A1_IN -> ADC_REFGND
- C37 pad 1: HVDD -> ADC_A6P
- C37 pad 2: A1_IN -> ADC_A6GND
- C38 pad 2: A1_IN -> ADC_REFGND
- C39 pad 2: A1_IN -> ADC_REFGND
- C4 pad 2: A1_IN -> ADC_REFGND
- C5 pad 2: A1_IN -> ADC_REFGND
- C51 pad 2: A1_IN -> ADC_REFGND
- C54 pad 2: A1_IN -> ADC_REFGND
- C55 pad 1: Net-(C55-Pad1) -> ADC_REF
- C55 pad 2: A1_IN -> ADC_REFGND
- C6 pad 2: A1_IN -> ADC_REFGND
- C60 pad 2: A1_IN -> ADC_A1GND
- C62 pad 1: ADC_A0 -> ADC_A1P
- C62 pad 2: A1_IN -> ADC_A1GND
- C7 pad 1: A1_IN -> ADC_REFGND
- C71 pad 1: ADC_C1 -> ADC_A4_OUT_N
- C71 pad 2: ADC_C0 -> ADC_A4_OUT_P
- C72 pad 1: ADC_B1 -> ADC_A2_OUT_N
- C72 pad 2: ADC_B0 -> ADC_A2_OUT_P
- C8 pad 1: A1_IN -> ADC_REFGND
- C9 pad 2: A1_IN -> ADC_REFGND
- D2 pad 2: A1_IN -> ADC_REFGND
- D3 pad 2: A1_IN -> ADC_REFGND
- D4 pad 2: A1_IN -> ADC_REFGND
- IC1 pad 2: A1_IN -> ADC_REFGND
- IC2 pad 3: A1_IN -> ADC_REFGND
- IC3 pad 11: 7P -> I2C1_SCL
- IC3 pad 13: 7N -> I2C1_SDA
- IC3 pad 14: A1_IN -> ADC_REFGND
- IC3 pad 17: A1_IN -> ADC_REFGND
- IC3 pad 2: A1_IN -> ADC_REFGND
- IC3 pad 20: A1_IN -> ADC_REFGND
- IC3 pad 3: A1_IN -> ADC_REFGND
- IC3 pad 4: A1_IN -> ADC_REFGND
- IC3 pad 7: A1_IN -> ADC_REFGND
- IC3 pad 9: 8P -> IRQ_TOUCH
- IC4 pad 1: A0_IN -> DIB_A0
- IC4 pad 2: A1_IN -> DIB_A1
- IC4 pad 3: A1_IN -> DIB_A2
- IC4 pad 4: B0_IN -> ADC_REFGND
- IC4 pad 5: B1_IN -> DIB_SDA
- IC4 pad 6: 5V -> DIB_SCL
- J3 pad 12: A1_IN -> ADC_REFGND
- J3 pad 15: A1_IN -> ADC_REFGND
- J3 pad 17: A2 -> DIB_A2
- J3 pad 18: A0 -> DIB_A0
- J3 pad 19: A1_IN -> ADC_REFGND
- J3 pad 2: (no net) -> DIB_+3V3
- J3 pad 20: A1 -> DIB_A1
- J3 pad 26: A1_IN -> ADC_REFGND
- J3 pad 3: 13N -> (no net)
- J3 pad 6: SSCL -> DIB_SCL
- J3 pad 7: SSDA -> DIB_SDA
- J3 pad 8: A1_IN -> ADC_REFGND
- J4 pad 1: A0_IN -> A1_IN
- J4 pad 10: B1_IN -> A2_IN_N
- J4 pad 12: (no net) -> ADC_REFGND
- J4 pad 2: B0_IN -> A2_IN_P
- J4 pad 4: (no net) -> A6_IN
- J4 pad 9: A1_IN -> ADC_REFGND
- J6 pad 1: (no net) -> I2C1_SDA
- J6 pad 2: (no net) -> 7N
- J6 pad 3: (no net) -> STM32_HSYNC
- J8 pad 1: +12V -> IRQ_TOUCH
- J8 pad 2: A1_IN -> 8P
- J8 pad 3: (no net) -> STM32_DE
- JP1 pad NC: 13N -> (no net)
- JP1 pad NO: A1_IN -> ADC_REFGND
- LCD_IN1 pad 13: A1_IN -> ADC_REFGND
- LCD_IN1 pad 14: A1_IN -> ADC_REFGND
- LCD_IN1 pad 21: A1_IN -> ADC_REFGND
- LCD_IN1 pad 22: A1_IN -> ADC_REFGND
- LCD_IN1 pad 29: A1_IN -> ADC_REFGND
- LCD_IN1 pad 3: A1_IN -> ADC_REFGND
- LCD_IN1 pad 32: /Video_IN/HSYNC -> STM32_HSYNC
- LCD_IN1 pad 34: /Video_IN/DE -> STM32_DE
- LCD_IN1 pad 36: /Video_IN/PWR_DWN -> (no net)
- LCD_IN1 pad 5: A1_IN -> ADC_REFGND
- LCD_IN1 pad 6: A1_IN -> ADC_REFGND
- LCD_OUT1 pad 13: A1_IN -> ADC_REFGND
- LCD_OUT1 pad 14: A1_IN -> ADC_REFGND
- LCD_OUT1 pad 21: A1_IN -> ADC_REFGND
- LCD_OUT1 pad 22: A1_IN -> ADC_REFGND
- LCD_OUT1 pad 29: A1_IN -> ADC_REFGND
- LCD_OUT1 pad 3: A1_IN -> ADC_REFGND
- LCD_OUT1 pad 5: A1_IN -> ADC_REFGND
- LCD_OUT1 pad 6: A1_IN -> ADC_REFGND
- R11 pad 1: Net-(C55-Pad1) -> ADC_REF
- R12 pad 1: ADC_REF -> Net-(R12-Pad1)
- R12 pad 2: Net-(C58-Pad1) -> 3V3
- R13 pad 1: ADC_REF -> DIB_+3V3
- R13 pad 2: Net-(C58-Pad2) -> DIB_A2
- R14 pad 1: 5V -> DIB_+3V3
- R14 pad 2: ADC_WORD -> DIB_A1
- R15 pad 1: ADC_WORD -> DIB_+3V3
- R15 pad 2: A1_IN -> DIB_A0
- R16 pad 1: 5V -> Net-(R16-Pad1)
- R16 pad 2: ADC_PAR -> 3V3
- R17 pad 1: ADC_PAR -> OS0
- R17 pad 2: A1_IN -> Net-(J10-Pad2)
- R18 pad 1: 5V -> OS1
- R18 pad 2: ADC_RANGE -> Net-(J11-Pad2)
- R19 pad 1: ADC_RANGE -> OS2
- R19 pad 2: A1_IN -> Net-(J12-Pad2)
- R2 pad 2: A1_IN -> ADC_REFGND
- R20 pad 1: 5V -> ADC_PAR
- R20 pad 2: ADC_REF_EN_WR -> Net-(J13-Pad2)
- R21 pad 1: ADC_REF_EN_WR -> ADC_RANGE
- R21 pad 2: A1_IN -> Net-(J14-Pad2)
- R22 pad 1: 5V -> ADC_REF_EN_WR
- R22 pad 2: ADC_HW_SW -> Net-(J15-Pad2)
- R23 pad 1: ADC_HW_SW -> ADC_STBY
- R23 pad 2: A1_IN -> 5V
- R25 pad 1: A1_IN -> ADC_REFGND
- R27 pad 1: ADC_A0 -> ADC_A1P
- R30 pad 2: B0_IN -> A2_IN_P
- R31 pad 2: B1_IN -> A2_IN_N
- R46 pad 1: ADC_C0 -> ADC_A4_OUT_P
- R47 pad 1: ADC_C1 -> ADC_A4_OUT_N
- R48 pad 1: ADC_B0 -> ADC_A2_OUT_P
- R49 pad 1: ADC_B1 -> ADC_A2_OUT_N
- R50 pad 1: 3V3 -> ADC_A1GND
- R50 pad 2: A2 -> ADC_REFGND
- R51 pad 1: 3V3 -> Net-(D5-Pad1)
- R51 pad 2: A1 -> A6_IN
- R52 pad 1: 3V3 -> ADC_A6P
- R52 pad 2: A0 -> Net-(D5-Pad1)
- R53 pad 2: A0_IN -> A1_IN
- TOUCH1 pad 1: A1_IN -> ADC_REFGND
- U1 pad 1: 18N -> 5V
- U1 pad 10: 22P -> 27P
- U1 pad 11: 22N -> 27N
- U1 pad 12: 23P -> 26P
- U1 pad 13: 23N -> 26N
- U1 pad 14: 24P -> 17N
- U1 pad 15: 24N -> 13N
- U1 pad 16: 25P -> 25N
- U1 pad 17: 25N -> 25P
- U1 pad 18: (no net) -> 24N
- U1 pad 19: 26N -> 19P
- U1 pad 2: 19P -> ADC_REFGND
- U1 pad 20: 26P -> 24P
- U1 pad 21: 27P -> 19N
- U1 pad 22: 27P -> 23N
- U1 pad 23: 27P -> 3V3
- U1 pad 24: 5V -> 20P
- U1 pad 25: A1_IN -> 23P
- U1 pad 26: 5V -> ADC_REFGND
- U1 pad 27: ADC_RANGE -> 20N
- U1 pad 28: 27N -> 22N
- U1 pad 29: ADC_WORD -> 21P
- U1 pad 3: 19N -> OS0
- U1 pad 30: HVSS -> 22P
- U1 pad 31: HVDD -> 21N
- U1 pad 32: A1_IN -> 18N
- U1 pad 33: ADC_A0 -> 18P
- U1 pad 34: 5V -> ADC_REF_EN_WR
- U1 pad 35: 5V -> ADC_REFGND
- U1 pad 36: (no net) -> Net-(C28-Pad2)
- U1 pad 37: A1_IN -> 5V
- U1 pad 38: A1_IN -> 5V
- U1 pad 39: ADC_B0 -> Net-(C27-Pad2)
- U1 pad 4: 20P -> OS1
- U1 pad 40: 5V -> ADC_REFGND
- U1 pad 41: 5V -> ADC_REFGND
- U1 pad 42: ADC_B1 -> ADC_REF
- U1 pad 43: A1_IN -> ADC_REFGND
- U1 pad 44: A1_IN -> Net-(C26-Pad1)
- U1 pad 45: ADC_C0 -> Net-(C26-Pad1)
- U1 pad 46: 5V -> ADC_REFGND
- U1 pad 47: 5V -> ADC_REFGND
- U1 pad 48: ADC_C1 -> 5V
- U1 pad 49: A1_IN -> ADC_A1P
- U1 pad 5: 20N -> OS2
- U1 pad 50: 5V -> ADC_A1GND
- U1 pad 51: ADC_REF -> ADC_A2_OUT_P
- U1 pad 52: A1_IN -> ADC_REFGND
- U1 pad 53: A1_IN -> ADC_A2_OUT_N
- U1 pad 54: Net-(C49-Pad2) -> ADC_REFGND
- U1 pad 55: A1_IN -> ADC_REFGND
- U1 pad 56: Net-(C48-Pad2) -> ADC_REFGND
- U1 pad 57: A1_IN -> ADC_A4_OUT_P
- U1 pad 58: Net-(C50-Pad2) -> (no net)
- U1 pad 59: A1_IN -> ADC_A4_OUT_N
- U1 pad 6: 21P -> ADC_PAR
- U1 pad 60: 5V -> (no net)
- U1 pad 61: ADC_PAR -> ADC_A6P
- U1 pad 62: ADC_HW_SW -> ADC_A6GND
- U1 pad 63: ADC_REF_EN_WR -> ADC_REFGND
- U1 pad 64: 18P -> ADC_REFGND
- U1 pad 7: 21N -> ADC_STBY
- U1 pad 8: (no net) -> ADC_RANGE
- U1 pad 9: 3V3 -> 27P
- U2 pad 4: A1_IN -> ADC_REFGND
- U2 pad 5: Net-(C53-Pad1) -> (no net)
- U3 pad 13: A1_IN -> ADC_REFGND
- U3 pad 18: A1_IN -> ADC_REFGND
- U3 pad 19: A1_IN -> ADC_REFGND
- U3 pad 21: A1_IN -> ADC_REFGND
- U3 pad 22: 13N -> Net-(R12-Pad1)
- U3 pad 25: A1_IN -> ADC_REFGND
- U3 pad 3: A1_IN -> ADC_REFGND
- U3 pad 32: A1_IN -> ADC_REFGND
- U3 pad 38: A1_IN -> ADC_REFGND
- U3 pad 44: A1_IN -> ADC_REFGND
- U3 pad 7: A1_IN -> ADC_REFGND
- U4 pad 11: A1_IN -> ADC_REFGND
- U4 pad 17: A1_IN -> ADC_REFGND
- U4 pad 22: /Video_IN/HSYNC -> STM32_HSYNC
- U4 pad 24: A1_IN -> ADC_REFGND
- U4 pad 25: /Video_IN/DE -> STM32_DE
- U4 pad 27: /Video_IN/PWR_DWN -> Net-(R16-Pad1)
- U4 pad 28: A1_IN -> ADC_REFGND
- U4 pad 30: A1_IN -> ADC_REFGND
- U4 pad 31: A1_IN -> ADC_REFGND
- U4 pad 32: Net-(C28-Pad2) -> 12P
- U4 pad 33: Net-(C32-Pad2) -> 12N
- U4 pad 34: Net-(C27-Pad2) -> 11P
- U4 pad 35: Net-(C31-Pad2) -> 11N
- U4 pad 36: A1_IN -> ADC_REFGND
- U4 pad 38: Net-(C26-Pad2) -> 10P
- U4 pad 39: Net-(C30-Pad2) -> 10N
- U4 pad 40: Net-(C25-Pad2) -> 9P
- U4 pad 41: Net-(C29-Pad2) -> 9N
- U4 pad 42: A1_IN -> ADC_REFGND
- U4 pad 46: A1_IN -> ADC_REFGND
- U4 pad 5: A1_IN -> ADC_REFGND
- U7 pad 6: A1_IN -> ADC_REFGND
- U8 pad 6: A1_IN -> ADC_REFGND
- ULX3S_L1 pad 21: A1_IN -> ADC_REFGND
- ULX3S_L1 pad 22: A1_IN -> ADC_REFGND
- ULX3S_L1 pad 3: A1_IN -> ADC_REFGND
- ULX3S_L1 pad 37: A1_IN -> ADC_REFGND
- ULX3S_L1 pad 38: A1_IN -> ADC_REFGND
- ULX3S_L1 pad 4: A1_IN -> ADC_REFGND
- ULX3S_R1 pad 19: A1_IN -> ADC_REFGND
- ULX3S_R1 pad 20: A1_IN -> ADC_REFGND
- ULX3S_R1 pad 29: (no net) -> 17P
- ULX3S_R1 pad 3: A1_IN -> ADC_REFGND
- ULX3S_R1 pad 30: (no net) -> 17N
- ULX3S_R1 pad 31: (no net) -> 16P
- ULX3S_R1 pad 32: (no net) -> 16N
- ULX3S_R1 pad 33: (no net) -> 15P
- ULX3S_R1 pad 34: (no net) -> 15N
- ULX3S_R1 pad 35: (no net) -> 14P
- ULX3S_R1 pad 36: (no net) -> 14N
- ULX3S_R1 pad 37: A1_IN -> ADC_REFGND
- ULX3S_R1 pad 38: A1_IN -> ADC_REFGND
- ULX3S_R1 pad 4: A1_IN -> ADC_REFGND
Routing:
- net ADC_REFGND: track 0.00 -> 927.9 mm, vias 0 -> 77
- net 5V: track 0.00 -> 447.1 mm, vias 0 -> 22
- net 3V3: track 0.00 -> 427.9 mm, vias 0 -> 40
- net +12V: track 0.00 -> 194.6 mm
- net 1P: track 0.00 -> 164.8 mm
- net 1N: track 0.00 -> 163.5 mm
- net 0P: track 0.00 -> 163.0 mm, vias 0 -> 1
- net 2P: track 0.00 -> 157.6 mm
- net 2N: track 0.00 -> 157.0 mm
- net 8N: track 0.00 -> 156.8 mm, vias 0 -> 1
- net 0N: track 0.00 -> 155.7 mm, vias 0 -> 1
- net VLED+: track 0.00 -> 149.7 mm, vias 0 -> 7
- net VLED-: track 0.00 -> 143.9 mm, vias 0 -> 7
- net 8P: track 0.00 -> 128.1 mm, vias 0 -> 1
- net 26P: track 0.00 -> 115.1 mm, vias 0 -> 2
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- added copper zone on F.Cu, net ADC_REFGND
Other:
- board size 215.1 x 95 mm -> 175.3 x 95.2 mm
